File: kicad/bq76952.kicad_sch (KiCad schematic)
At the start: 92 parts, among them Q1 DMN10H220LE, Q13 BSS123N, U4 BQ76952

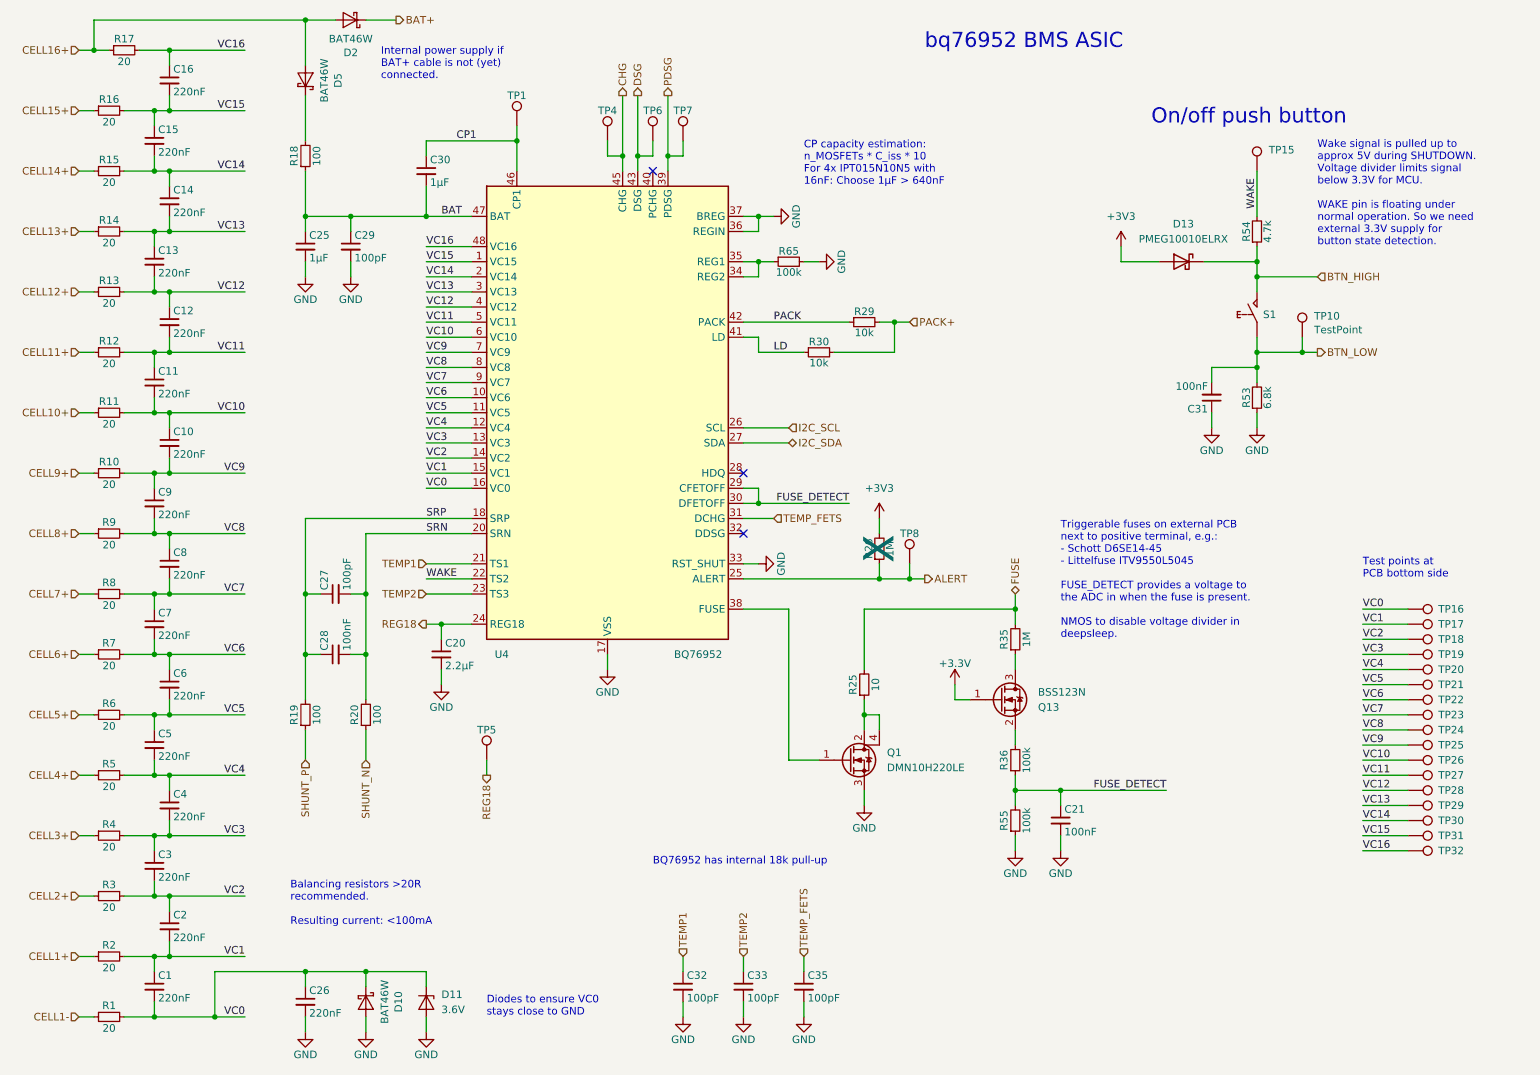
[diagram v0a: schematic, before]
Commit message: Remove FUSE_DETECT circuit
Q13 was not properly tied to ground, so it was not switching on the
voltage divider. A voltage divider that is continuously on would
draw current even in deepsleep mode, so it is not viable for a BMS.

I could not come up with an easy circuit that allows monitoring the
voltage without any power consumption, so the fuse diagnosis
mechanism is removed for now.
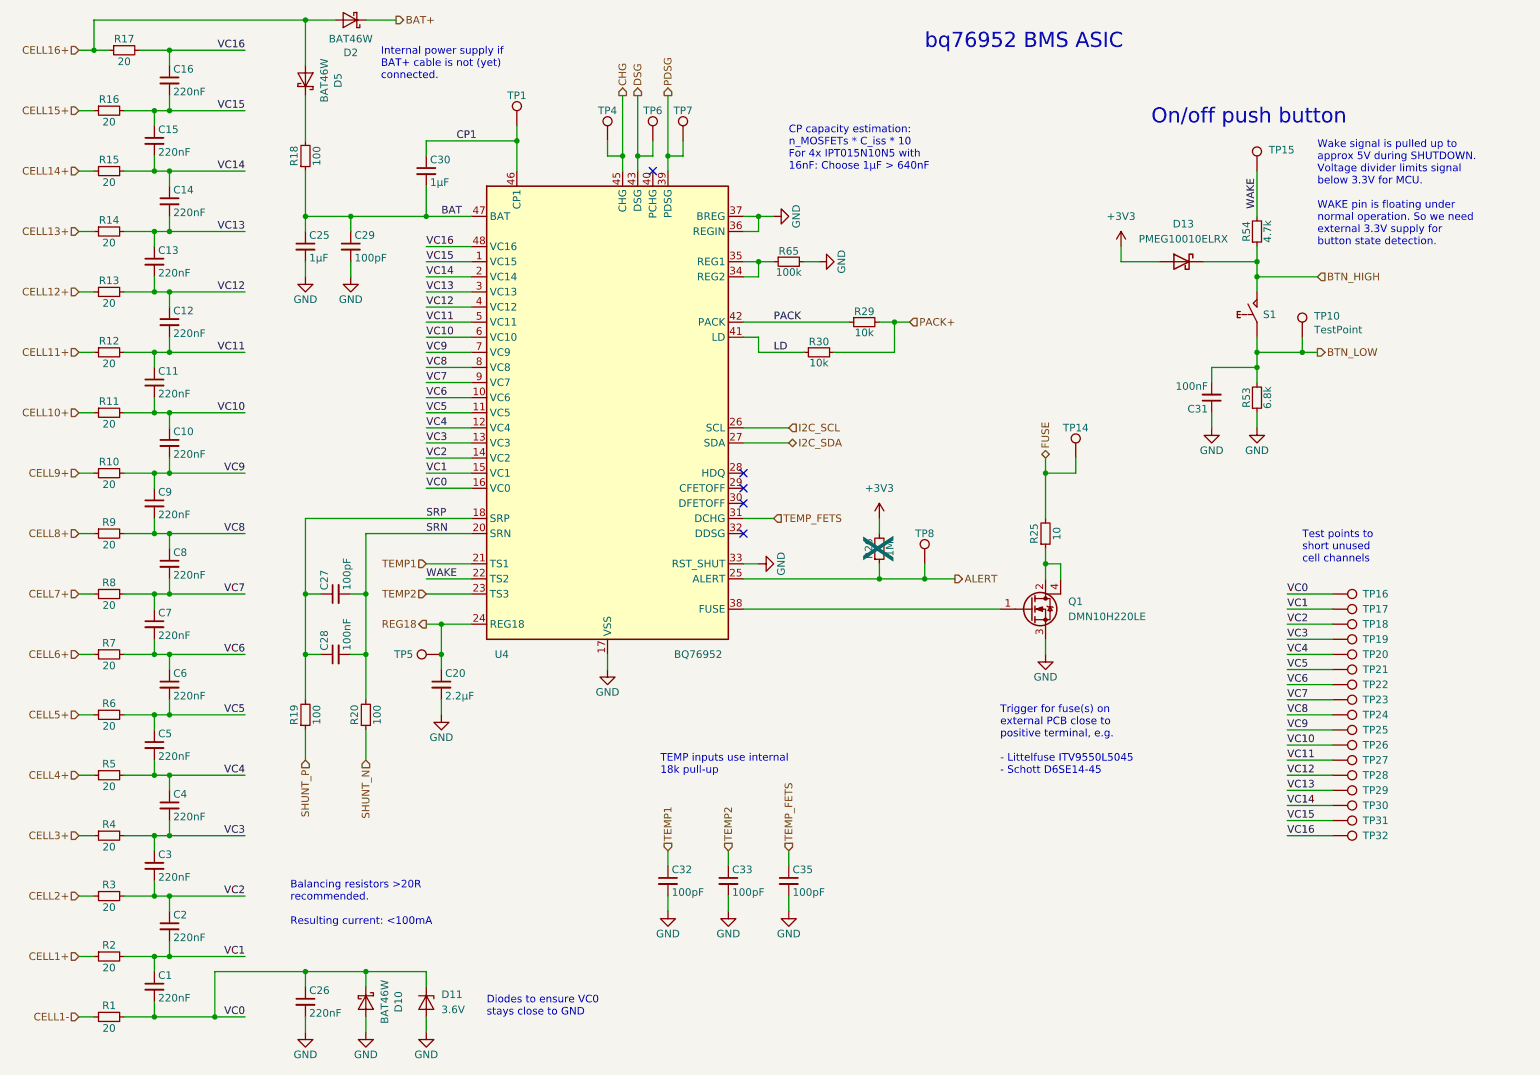
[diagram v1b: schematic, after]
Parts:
- removed C21: 100nF, LibreSolar:C_0603_1608, symbol LibreSolar:C
- removed Q13: BSS123N, LibreSolar:SOT-23, symbol Device:Q_NMOS_GSD
- removed R35: 1M, LibreSolar:R_0603_1608, symbol LibreSolar:R
- removed R36, R55: 100k, LibreSolar:R_0603_1608, symbol LibreSolar:R
- added TP14: TestPoint, TestPoint:TestPoint_Pad_D1.5mm, symbol Connector:TestPoint
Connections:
- net FUSE: now also TP14.1
- net FUSE_DETECT: no longer names the net of U4.29 (CFETOFF)
- net FUSE_DETECT: no longer U4.30 (DFETOFF)
- no-connect marks 3 -> 5
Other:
- note added: "TEMP inputs use internal 18k pull-up"
- note added: "Test points to short unused cell channels"
- note added: "Trigger for fuse(s) on external PCB close to positive terminal, e.g. - Littelfuse ITV9550L5045 - Schott D6SE14-45"
- note removed: "BQ76952 has internal 18k pull-up"
- note removed: "Test points at PCB bottom side"
- note removed: "Triggerable fuses on external PCB next to positive terminal, e.g.: - Schott D6SE14-45 - Littelfuse ITV9550L5045 FUSE_DETECT provides a voltage to the ADC in when the fuse is present. NMOS to disable voltage divider in deepsleep."
- moved on the sheet: C20, C32, C33, C35, Q1, R25, TP16, TP17, TP18, TP19, TP20, TP21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

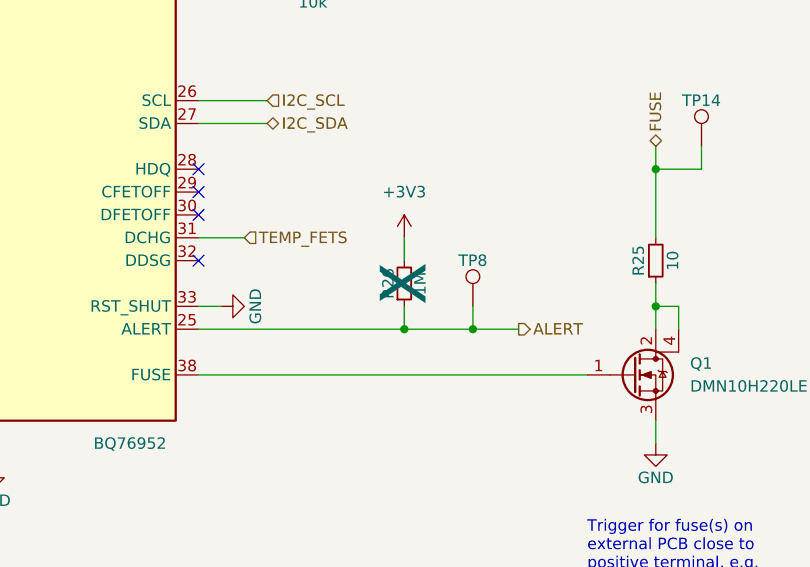
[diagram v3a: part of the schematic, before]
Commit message: v0.3.3: Final version for BMS challenge with EnAccess
Updates compared to v0.3.2:

- Optimization of some copper planes
- Net tie with thicker connection to GND
- D12 connected to Bat-

No parts were changed, the BOM is same as before.
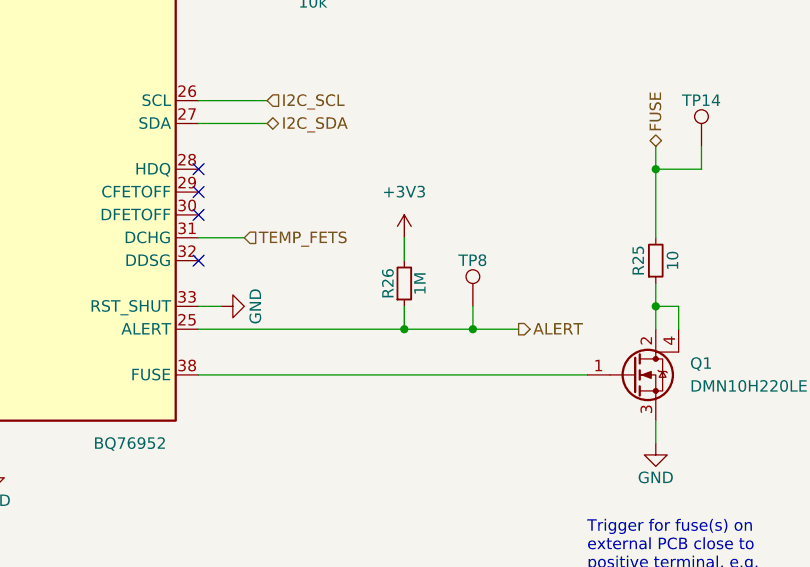
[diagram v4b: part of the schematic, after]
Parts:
- R26: DNM X -> (none)
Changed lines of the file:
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@@
   (title_block
     (title "Libre Solar BMS C1")
-    (date "2022-11-07")
-    (rev "0.3.2")
+    (date "2022-11-21")
+    (rev "0.3.3")
     (company "Libre Solar Technologies GmbH")
     (comment 1 "Website: https://libre.solar")
@@
       (effects (font (size 1.27 1.27)) hide)
     )
-    (property "Reference" "TP32" (id 5) (at 248.92 154.94 0)
-      (effects (font (size 1.27 1.27)) hide)
-    )
-    (property "Value" "TestPoint" (id 6) (at 248.92 154.94 0)
-      (effects (font (size 1.27 1.27)) hide)
-    )
     (pin "1")
   )
@@
       (effects (font (size 1.27 1.27)) hide)
     )
-    (property "PartNumber" "" (id 5) (at 50.8 -29.21 0)
-      (effects (font (size 1.27 1.27)) hide)
-    )
-    (property "DNM" "X" (id 6) (at 172.72 106.68 90)
-      (effects (font (size 5.08 5.08)))
-    )
     (pin "1")
     (pin "2")
@@
     )
     (property "PartNumber" "MMSZ4685T1G" (id 5) (at 96.52 182.88 0)
-      (effects (font (size 1.27 1.27)) hide)
-    )
-    (property "Reference" "D11" (id 6) (at 96.52 182.88 0)
-      (effects (font (size 1.27 1.27)) hide)
-    )
-    (property "Value" "3.6V" (id 7) (at 96.52 182.88 0)
       (effects (font (size 1.27 1.27)) hide)
     )
@@
       (effects (font (size 1.27 1.27)) hide)
     )
-    (property "Reference" "Q1" (id 8) (at 198.12 116.84 0)
-      (effects (font (size 1.27 1.27)) hide)
-    )
-    (property "Value" "DMN10H220LE" (id 9) (at 198.12 116.84 0)
-      (effects (font (size 1.27 1.27)) hide)
-    )

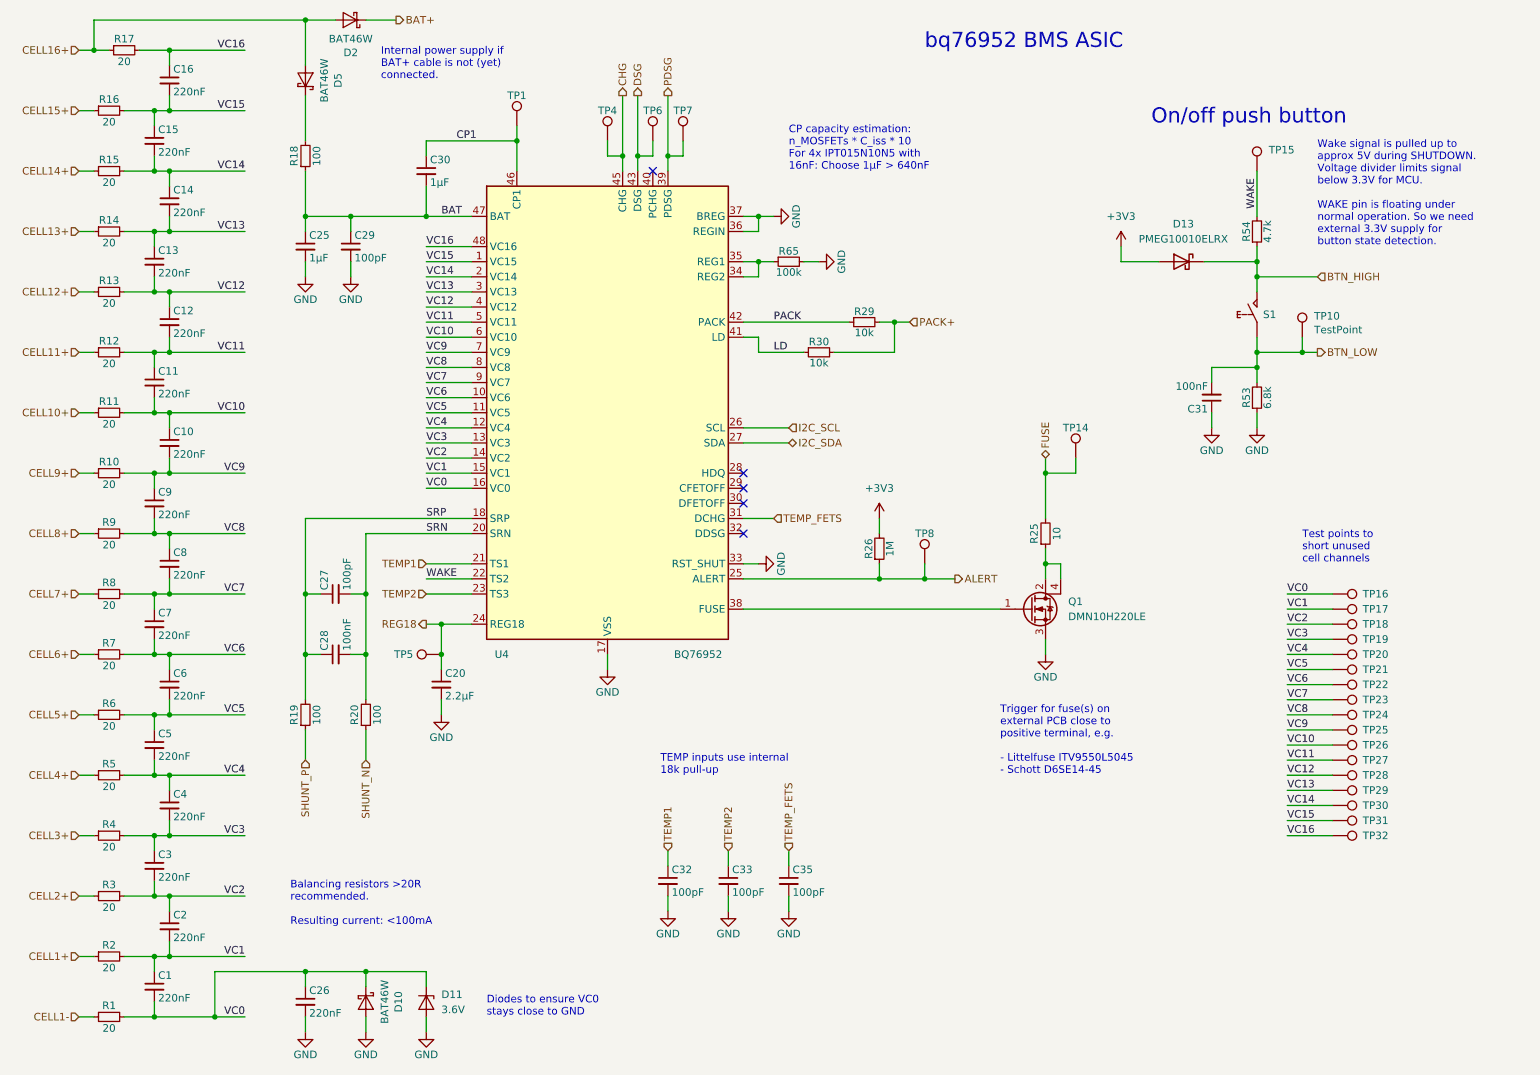
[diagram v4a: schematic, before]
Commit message: v0.4.0: Multiple improvements for new board revision
- Use LMR38010 for internal power supply (max. 80V instead of 60V)
- Change USB connector from Micro-A to C and remove 5V power supply
  which was not working anyway. The board cannot be powered by USB
  only.
- Add TS2 (connected to DFETOFF) to measure shunt temperature
- Add RS-485 transceiver (sharing the connector with CAN)
- Switch I2C pins of ESP32-C3 to GPIO8/9. This allows to re-use the
  I2C pull-ups for strapping configuration and frees two pins for the
  RS-485 transceiver RE and DE pins. Also we may get rid of the I2C
  glitches during start-up.
- Use 80V instead of 100V power MOSFETs to reduce Rds(on).
- Reduce DSG gate resistor R57 to 47R to increase switch-off speed.
- Adjust some resistors to reduce number of different parts
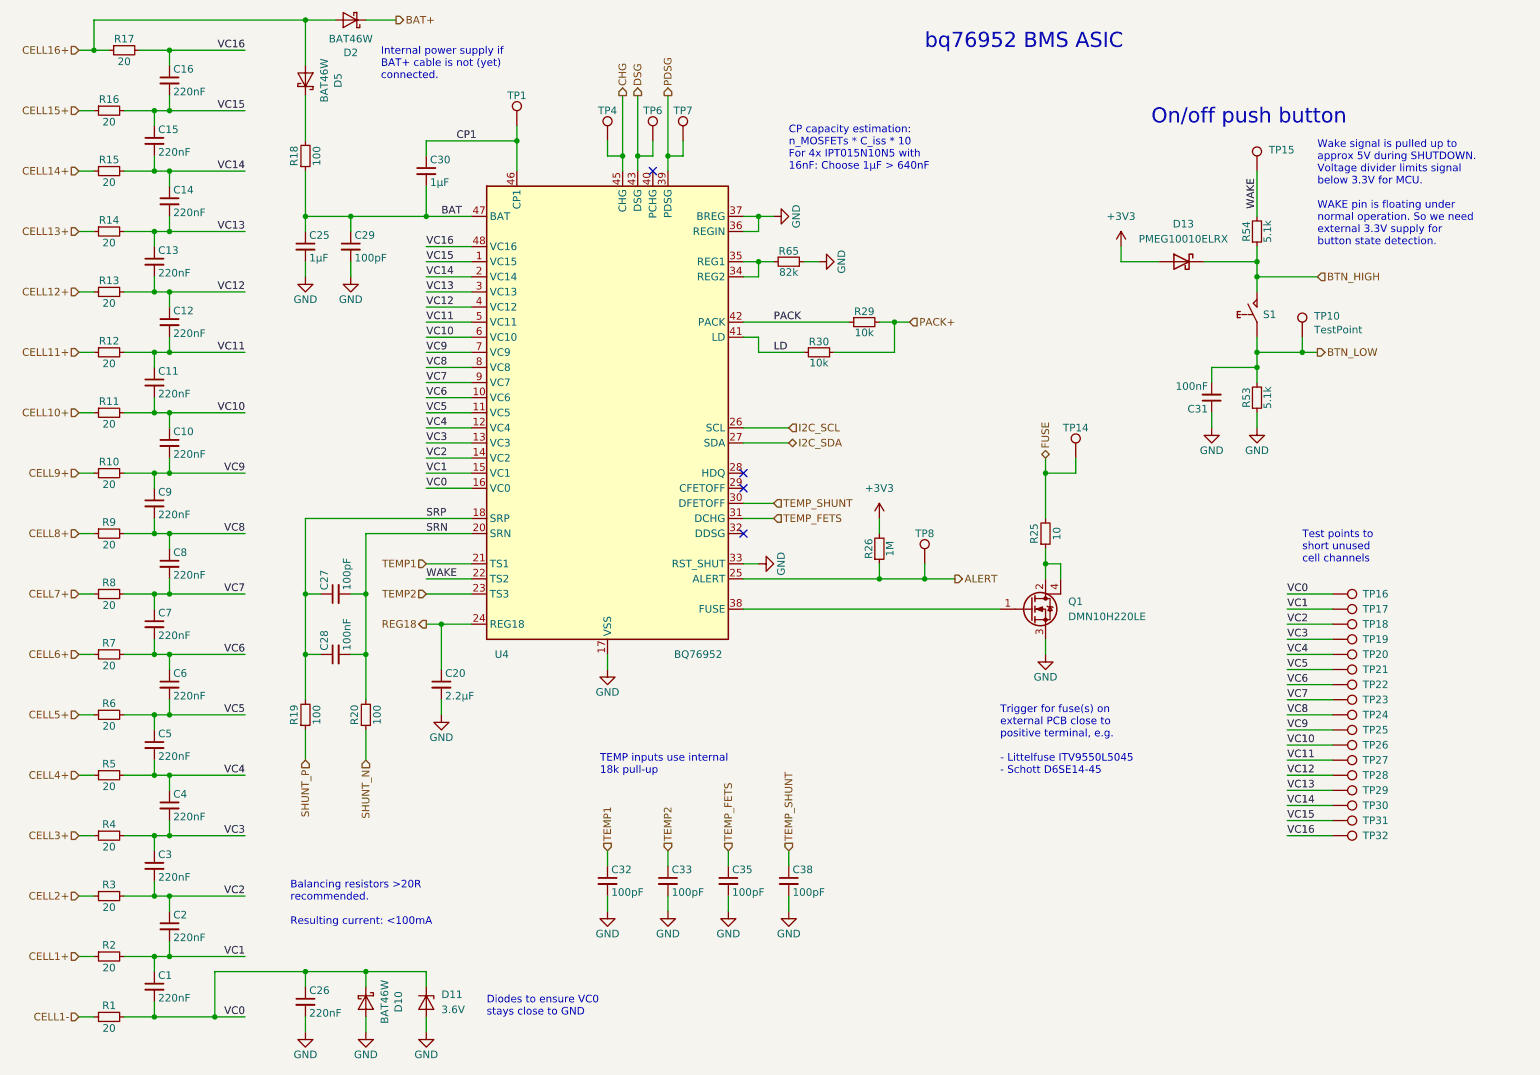
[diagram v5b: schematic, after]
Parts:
- removed TP5: TestPoint, TestPoint:TestPoint_Pad_D1.5mm, symbol Connector:TestPoint
- added C38: 100pF, LibreSolar:C_0603_1608, symbol LibreSolar:C
- C1, C10, C11, C12, C13, C14, C15, C16, C2, C26, C3, C4, C5, C6, C7, C8, C9: LCSC (none) -> C21120; Manufacturer any -> Samsung Electro-Mechanics; PartNumber (none) -> CL10B224KA8NNNC; Remarks (none) -> min. 25V, X7R
- C20: LCSC (none) -> C1607; Manufacturer any -> Samsung Electro-Mechanics; PartNumber (none) -> CL10A225KP8NNNC; Remarks X7R, 10V -> min. 10V, X7R
- C25: LCSC (none) -> C13832; Manufacturer any -> Samsung Electro-Mechanics; PartNumber (none) -> CL31B105KCHNNNE; Remarks 100V, X7R -> min. 100V, X5R
- C27, C29, C32, C33, C35: LCSC (none) -> C296717; Manufacturer any -> Samsung Electro-Mechanics; PartNumber (none) -> CL10C101JC8NNNC
- C28, C31: LCSC (none) -> C15725; Manufacturer any -> Samsung Electro-Mechanics; PartNumber (none) -> CL10B104KC8NNNC; Remarks X7R, 100V -> min. 100V, X7R
- C30: LCSC (none) -> C5673; Manufacturer any -> Samsung Electro-Mechanics; PartNumber (none) -> CL10A105KA8NNNC; Remarks 25V, X5R -> min. 25V, X5R
- D10, D2, D5: LCSC (none) -> C83152
- D11: LCSC (none) -> C66886
- D13: LCSC (none) -> C179426
- Q1: LCSC (none) -> C258216
- R1, R10, R11, R12, R13, R14, R15, R16, R17, R2, R3, R4, R5, R6, R7, R8, R9: LCSC (none) -> C163344
- R18: Manufacturer any -> Yageo; PartNumber (none) -> RC1206FR-07100RL
- R19, R20: Manufacturer any -> Yageo; PartNumber (none) -> RC0603FR-07100RL
- R25: Manufacturer any -> Yageo; PartNumber (none) -> RC1206FR-0710RL
- R26: Manufacturer any -> Yageo; PartNumber (none) -> RC0603FR-071ML
- R29, R30: Manufacturer any -> Yageo; PartNumber (none) -> RC0603FR-0710KL
- R53: value 6.8k -> 5.1k; Manufacturer any -> Yageo; PartNumber (none) -> RC0603FR-075K1L
- R54: value 4.7k -> 5.1k; Manufacturer any -> Yageo; PartNumber (none) -> RC0603FR-075K1L
- R65: value 100k -> 82k; Manufacturer any -> Yageo; PartNumber (none) -> RC0603FR-0782KL
- U4: LCSC (none) -> C2862742
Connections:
- net GND: now also C38.2
- net TEMP_SHUNT: now reaches U4.30 (DFETOFF)
- net TEMP_SHUNT: now also C38.1
- no-connect marks 5 -> 4
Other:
- moved on the sheet: C32, C33, C35

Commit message: Update files to KiCad v8
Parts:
- S1: LCSC (none) -> C2886899
